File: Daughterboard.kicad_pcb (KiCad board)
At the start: 4 copper layers, 60 parts, among them U1 SI8271GB-IS, U2 SI8271GB-IS, U3 GS61004B, U4 IES0105S09, U5 GS61004B, U6 IES0105S09

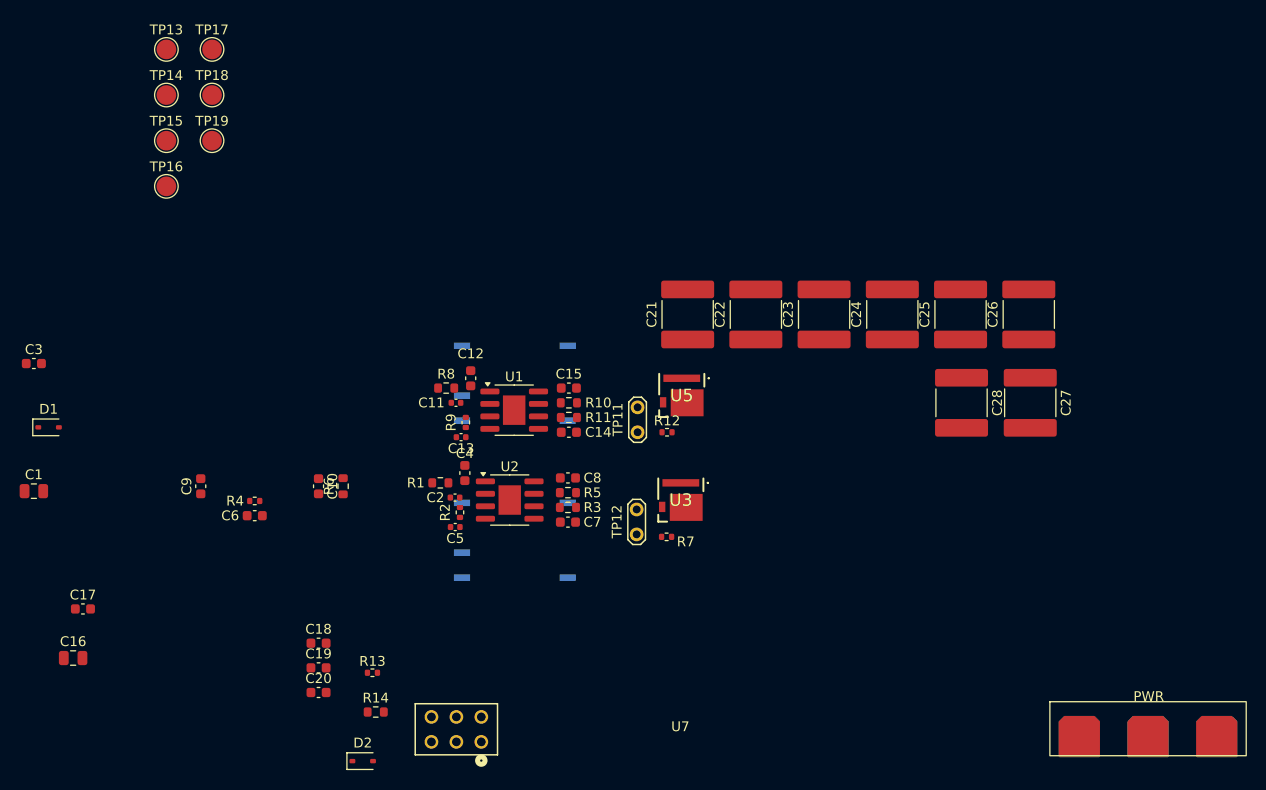
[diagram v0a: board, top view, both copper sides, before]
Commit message: start layout design, component placement
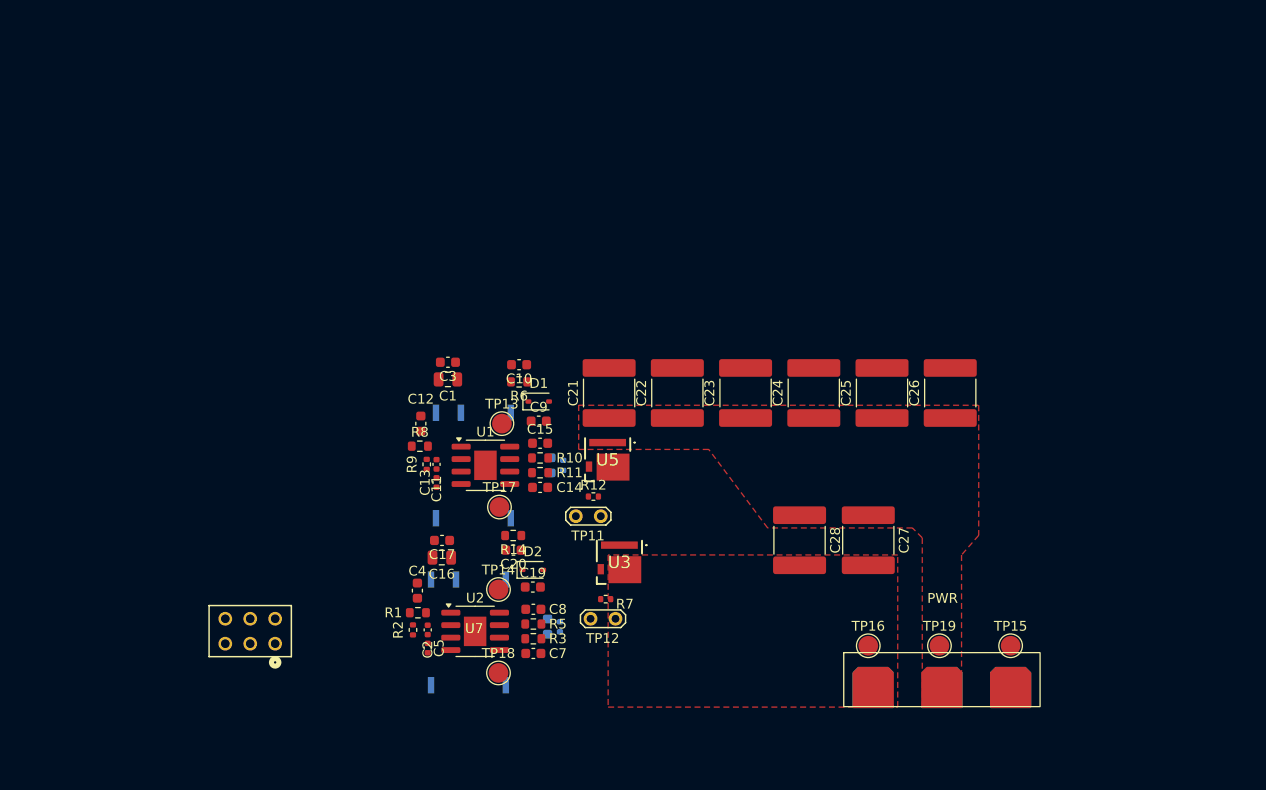
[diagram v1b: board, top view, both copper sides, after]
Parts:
- C18, C6, R13, R4: moved to B.Cu
- moved TP15 100.2 mm to (161.0, 121.2)
- moved TP19 90.2 mm to (153.8, 121.2)
- moved TP16 85.5 mm to (146.5, 121.2)
- moved TP18 65.7 mm to (108.8, 124.0)
- moved TP14 60.7 mm to (108.8, 115.5)
- moved TP17 55.1 mm to (108.9, 107.1)
- moved TP13 51.2 mm to (109.2, 98.6)
- moved D1 50.0 mm to (112.9, 96.4)
- moved C1 43.7 mm to (103.7, 94.1), turned to 180 degrees
- moved C3 42.2 mm to (103.7, 92.4), turned to 180 degrees
- moved C16 38.9 mm to (103.1, 112.3), turned to 180 degrees
- moved C17 37.2 mm to (103.1, 110.5), turned to 180 degrees
- moved C9 35.1 mm to (112.9, 98.4), turned to 0 degrees
- moved R4 31.6 mm to (115.4, 102.9), turned to 90 degrees
- moved C6 30.6 mm to (114.2, 102.9), turned to 90 degrees
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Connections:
- U7 pad 7: DC+ -> DC-
- U7 pad 8: SW -> DC+
- U7 pad 9: DC- -> SW
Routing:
- added copper zone on F.Cu, net DC+
- added copper zone on F.Cu, net DC-

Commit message: initial version for commenting
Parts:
- C18, C6, R13, R4: moved to F.Cu
- TP13, TP14, TP15, TP16, TP17, TP18, TP19: footprint TestPoint:TestPoint_Pad_D2.0mm -> TestPoint:TestPoint_THTPad_D1.0mm_Drill0.5mm
- U3, U5: footprint GS61004B:GS61004B -> GS61004B:GS6XXX4B
- moved TP17 13.4 mm to (110.5, 93.8)
- moved TP18 13.0 mm to (109.7, 111.0)
- moved C7 12.5 mm to (112.4, 109.5)
- moved C14 12.4 mm to (112.9, 92.7)
- moved C11 8.32 mm to (101.6, 94.5), turned to 180 degrees
- moved C2 8.14 mm to (101.4, 111.5), turned to 180 degrees
- moved R13 8.03 mm to (108.0, 123.1), turned to 0 degrees
- moved C18 7.29 mm to (107.8, 115.2)
- moved R4 7.27 mm to (109.5, 107.0), turned to 180 degrees
- moved C6 6.83 mm to (109.1, 98.3)
- moved C1 4.09 mm to (101.5, 97.5)
- moved C3 3.94 mm to (101.7, 95.8)
- moved C16 2.82 mm to (101.2, 114.4)
- moved C17 2.81 mm to (101.3, 112.7)
- moved C10 2.53 mm to (112.9, 94.2)
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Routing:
- net ENABLEH: track 0.00 -> 30.1 mm, vias 0 -> 1
- net PWMH: track 0.00 -> 29.4 mm, vias 0 -> 1
- net PWML: track 0.00 -> 20.8 mm, vias 0 -> 1
- net ENABLEL: track 0.00 -> 20.1 mm, vias 0 -> 1
- net VDDL: track 0.00 -> 13.4 mm, vias 0 -> 1
- net VEEH: track 0.00 -> 12.3 mm, vias 0 -> 3
- net VDDH: track 0.00 -> 11.2 mm, vias 0 -> 1
- net VEEL: track 0.00 -> 8.90 mm, vias 0 -> 3
- net VCC+5V: track 0.00 -> 5.98 mm, vias 0 -> 10
- net GND: track 0.00 -> 5.78 mm, vias 0 -> 7
- net Net-(U2-VI): track 0.00 -> 4.13 mm
- net Net-(U1-VI): track 0.00 -> 3.98 mm
- net DC-: track 0.00 -> 2.74 mm, vias 0 -> 220
- net Net-(U2-VO-): track 0.00 -> 2.68 mm
- net Net-(U2-VO+): track 0.00 -> 2.68 mm
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- added copper zone on B.Cu, net /VgH
- added copper zone on F.Cu, net /VgH
- added copper zone on B.Cu, net /VgL
- added copper zone on F.Cu, net /VgL
- added copper zone on B.Cu, net DC+
- added copper zone on B.Cu, net DC-
- added copper zone on In1.Cu, net DC-
- added copper zone on In2.Cu, net DC-
- added copper zone on B.Cu, net GND
- added copper zone on F.Cu, net GND
- added copper zone on B.Cu, net SW
- added copper zone on F.Cu, net SW
- added copper zone on In1.Cu, net SW
- added copper zone on In2.Cu, net SW
- added copper zone on B.Cu, net VCC+5V
- added copper zone on F.Cu, net VCC+5V
- added copper zone on F.Cu, net VDDH
- added copper zone on F.Cu, net VDDL
- added copper zone on B.Cu, net VEEH
- added copper zone on F.Cu, net VEEH
- added copper zone on B.Cu, net VEEL
- added copper zone on F.Cu, net VEEL
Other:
- board outline added: 85.6 x 38.5 mm

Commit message: fixed after comments
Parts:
- added 6: Conn_02x03_Odd_Even, 3x2_connector:CON6_2X3_TU_TSW_SAI, F.Cu at (93.8, 95.9)
- U1, U2: footprint Package_SO:SOIC-8-1EP_3.9x4.9mm_P1.27mm_EP2.29x3mm -> Package_SO:SOIC-8_3.9x4.9mm_P1.27mm
- moved VgLDC- 34.1 mm to (104.7, 90.6)
- moved DC- 33.3 mm to (163.4, 90.6)
- moved VDDL 27.7 mm to (99.4, 90.6)
- moved DC+ 26.5 mm to (163.4, 94.6)
- moved VEEL 24.0 mm to (97.1, 90.6)
- moved SW 21.3 mm to (163.4, 98.2)
- moved SW 19.6 mm to (114.3, 90.6), turned to 0 degrees
- moved C14 14.0 mm to (114.4, 106.6)
- moved C7 11.0 mm to (114.8, 120.2)
- moved R13 10.0 mm to (110.9, 113.5), turned to 90 degrees
- moved U7 9.96 mm to (91.1, 118.6)
- moved C11 9.37 mm to (104.4, 103.5), turned to -90 degrees
- moved VgL 9.34 mm to (107.2, 90.5)
- moved R4 8.10 mm to (111.0, 99.0), turned to 90 degrees
- moved C2 6.81 mm to (104.4, 117.6), turned to -90 degrees
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- renumbered TP19 to DC+, TP16 to DC-, TP15 to SW, TP11 to SW, TP14 to VDDL, TP17 to VEEH, TP18 to VEEL, TP13 to VgL, TP12 to VgLDC-
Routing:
- net /VgL: track 0.00 -> 37.7 mm, vias 9 -> 1
- net VDDL: track 13.4 -> 39.5 mm, vias 1 -> 3
- net DC-: track 2.74 -> 24.3 mm, vias 220 -> 219
- net VEEL: track 8.90 -> 29.9 mm, vias 3 -> 4
- net PWML: track 20.8 -> 39.6 mm, vias 1 -> 0
- net ENABLEH: track 30.1 -> 45.6 mm, vias 1 -> 0
- net ENABLEL: track 20.1 -> 35.3 mm, vias 1 -> 0
- net /VgH: track 0.00 -> 13.2 mm, vias 4 -> 1
- net DC+: track 0.00 -> 8.85 mm, vias 0 -> 9
- net SW: track 0.00 -> 8.48 mm, vias 70 -> 69
- net VEEH: track 12.3 -> 5.79 mm, vias 3 -> 4
- net VCC+5V: track 5.98 -> 0.00 mm, vias 10 -> 12
- net GND: track 5.78 -> 0.00 mm, vias 7 -> 6
- net PWMH: track 29.4 -> 34.9 mm, vias 1 -> 0
- net Net-(U2-VI): track 4.13 -> 0.00 mm
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- added copper zone on In1.Cu, net GND
- added copper zone on F.Cu, net Net-(U1-VI)
- added copper zone on F.Cu, net Net-(U2-VI)
- added copper zone on In2.Cu, net VCC+5V
- added copper zone on B.Cu, net VDDH
- added copper zone on B.Cu, net VDDL
- added copper zone on In2.Cu, net VEEH
- added copper zone on In2.Cu, net VEEL
- removed copper zone on B.Cu, net /VgH
- removed copper zone on B.Cu, net /VgL
- removed copper zone on In2.Cu, net SW
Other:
- board size 85.6 x 38.5 mm -> 76 x 38.5 mm
- board text added: "VgH"

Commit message: second version after comments
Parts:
- VgL DC-: renamed from VgLDC-
- moved VEEL 8.70 mm to (105.8, 90.4)
- moved VDDL 6.68 mm to (105.8, 92.5)
- moved VgL 4.60 mm to (111.8, 90.4)
- moved VEEH 2.97 mm to (111.8, 92.5)
- moved VgL DC- 1.70 mm to (103.0, 90.6)
- renumbered 6 to GND
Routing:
- net VDDL: track 39.5 -> 24.6 mm
- net VEEL: track 29.9 -> 21.3 mm
- net VEEH: track 5.79 -> 2.10 mm
- net DC-: track 24.3 -> 26.3 mm
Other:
- board size 76 x 38.5 mm -> 76 x 38.9 mm
- board text added: "EN_H"
- board text added: "EN_L"
- board text added: "PWMH"
- board text added: "PWML"
- board text added: "VCC"

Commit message: gerbers, drill files and pick-and-place added, deleted unneccessary items from BOM
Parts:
- renumbered VgL to VDDH
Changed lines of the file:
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@@
 			(plot_on_all_layers_selection 0x0000000_00000000)
 			(disableapertmacros no)
-			(usegerberextensions no)
-			(usegerberattributes yes)
-			(usegerberadvancedattributes yes)
-			(creategerberjobfile yes)
+			(usegerberextensions yes)
+			(usegerberattributes no)
+			(usegerberadvancedattributes no)
+			(creategerberjobfile no)
 			(dashed_line_dash_ratio 12.000000)
 			(dashed_line_gap_ratio 3.000000)
@@
 			(psa4output no)
 			(plotreference yes)
-			(plotvalue yes)
+			(plotvalue no)
 			(plotfptext yes)
 			(plotinvisibletext no)
 			(sketchpadsonfab no)
-			(subtractmaskfromsilk no)
+			(subtractmaskfromsilk yes)
 			(outputformat 1)
 			(mirror no)
-			(drillshape 1)
+			(drillshape 0)
 			(scaleselection 1)
-			(outputdirectory "")
+			(outputdirectory "gerbers/")
 		)
 	)
@@
 		(tags "resistor")
 		(property "Reference" "R13"
-			(at 0.1 -1.3 270)
+			(at 0.1 -1.3 -90)
 			(layer "F.SilkS")
 			(effects
@@
 		)
 		(property "Value" "2.2k"
-			(at 0 1.17 270)
+			(at 0 1.17 -90)
 			(layer "F.Fab")
 			(effects
@@
 		)
 		(fp_text user "${REFERENCE}"
-			(at 0 0 270)
+			(at 0 0 -90)
 			(layer "F.Fab")
 			(effects
@@
 		)
 		(property "Value" "1k"
-			(at 0 1.43 270)
+			(at 0 1.43 -90)
 			(layer "F.Fab")
 			(effects
@@
 		)
 		(fp_text user "${REFERENCE}"
-			(at 0 0 270)
+			(at 0 0 -90)
 			(layer "F.Fab")
 			(effects
@@
 		)
 		(property "Value" "1u 50 V"
-			(at 0 1.43 270)
+			(at 0 1.43 -90)
 			(layer "F.Fab")
 			(effects
@@
 		)
 		(fp_text user "${REFERENCE}"
-			(at 0 0 270)
+			(at 0 0 -90)
 			(layer "F.Fab")
 			(effects
@@
 		(descr "THT pad as test Point, diameter 1.0mm, hole diameter 0.5mm")
 		(tags "test point THT pad")
-		(property "Reference" "VgL"
-			(at -2 -0.1 90)
+		(property "Reference" "VDDH"
+			(at -2 0.4 90)
 			(layer "F.SilkS")
 			(effects
@@
 		)
 		(fp_text user "${REFERENCE}"
-			(at 0 0 270)
+			(at 0 0 -90)
 			(layer "F.Fab")
 			(effects
@@
 		)
 		(fp_text user "${REFERENCE}"
-			(at 0 0 270)
+			(at 0 0 -90)
 			(layer "F.Fab")
 			(effects
@@
 		)
 		(property "Value" "1u 50 V"
-			(at 0 1.43 270)
+			(at 0 1.43 -90)
 			(layer "F.Fab")
 			(effects
@@
 		)
 		(fp_text user "${REFERENCE}"
-			(at 0 0 270)
+			(at 0 0 -90)
 			(layer "F.Fab")
 			(effects
@@
 		)
 		(property "Value" "0.1u 50 V"
-			(at 0 1.16 270)
+			(at 0 1.16 -90)
 			(layer "F.Fab")
 			(effects
@@
 		)
 		(fp_text user "${REFERENCE}"
-			(at 0 0 270)
+			(at 0 0 -90)
 			(layer "F.Fab")
 			(effects
@@
 		(tags "capacitor")
 		(property "Reference" "C10"
-			(at 0 -1.3 270)
+			(at 0 -1.3 -90)
 			(layer "F.SilkS")
 			(effects
@@
 		)
 		(property "Value" "1u 50 V"
-			(at 0 1.43 270)
+			(at 0 1.43 -90)
 			(layer "F.Fab")
 			(effects
@@
 		)
 		(fp_text user "${REFERENCE}"
-			(at 0 0 270)
+			(at 0 0 -90)
 			(layer "F.Fab")
 			(effects
@@
 		)
 		(property "Value" "5.8"
-			(at 0.1 1.9 270)
+			(at 0.1 1.9 -90)
 			(layer "F.Fab")
 			(effects
@@
 		)
 		(fp_text user "${REFERENCE}"
-			(at 0 -1.85 270)
+			(at 0 -1.85 -90)
 			(layer "F.Fab")
 			(effects
@@
 		)
 		(property "Value" "5.8"
-			(at 0.1 1.9 270)
+			(at 0.1 1.9 -90)
 			(layer "F.Fab")
 			(effects
@@
 		)
 		(fp_text user "${REFERENCE}"
-			(at 0 -1.85 270)
+			(at 0 -1.85 -90)
 			(layer "F.Fab")
 			(effects
@@
 		)
 		(property "Value" "TestPoint_2Pole"
-			(at 1.27 2 360)
+			(at 1.27 2 0)
 			(layer "F.Fab")
 			(effects
@@
 		(tags "resistor")
 		(property "Reference" "R14"
-			(at 0 1.6 270)
+			(at 0 1.6 -90)
 			(layer "F.SilkS")
 			(effects
@@
 		)
 		(property "Value" "1k"
-			(at 0 1.43 270)
+			(at 0 1.43 -90)
 			(layer "F.Fab")
 			(effects
@@
 		)
 		(fp_text user "${REFERENCE}"
-			(at 0 0 270)
+			(at 0 0 -90)
 			(layer "F.Fab")
 			(effects
@@
 		)
 		(property "Value" "1u 50 V"
-			(at 0 1.43 270)
+			(at 0 1.43 -90)
 			(layer "F.Fab")
 			(effects
@@
 		)
 		(fp_text user "${REFERENCE}"
-			(at 0 0 270)
+			(at 0 0 -90)
 			(layer "F.Fab")
 			(effects
